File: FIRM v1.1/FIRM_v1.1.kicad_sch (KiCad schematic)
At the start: 79 parts, among them J2 Conn_01x02_Pin, Q1 IRLML6402, U10 STM32F446ZCHx, U3 ADXL371, U5 INA219AxDCN, U6 MIC5219-3.3YM5, U9 A-USBC-20F0-EA-GSR05, Y2 12 MHz

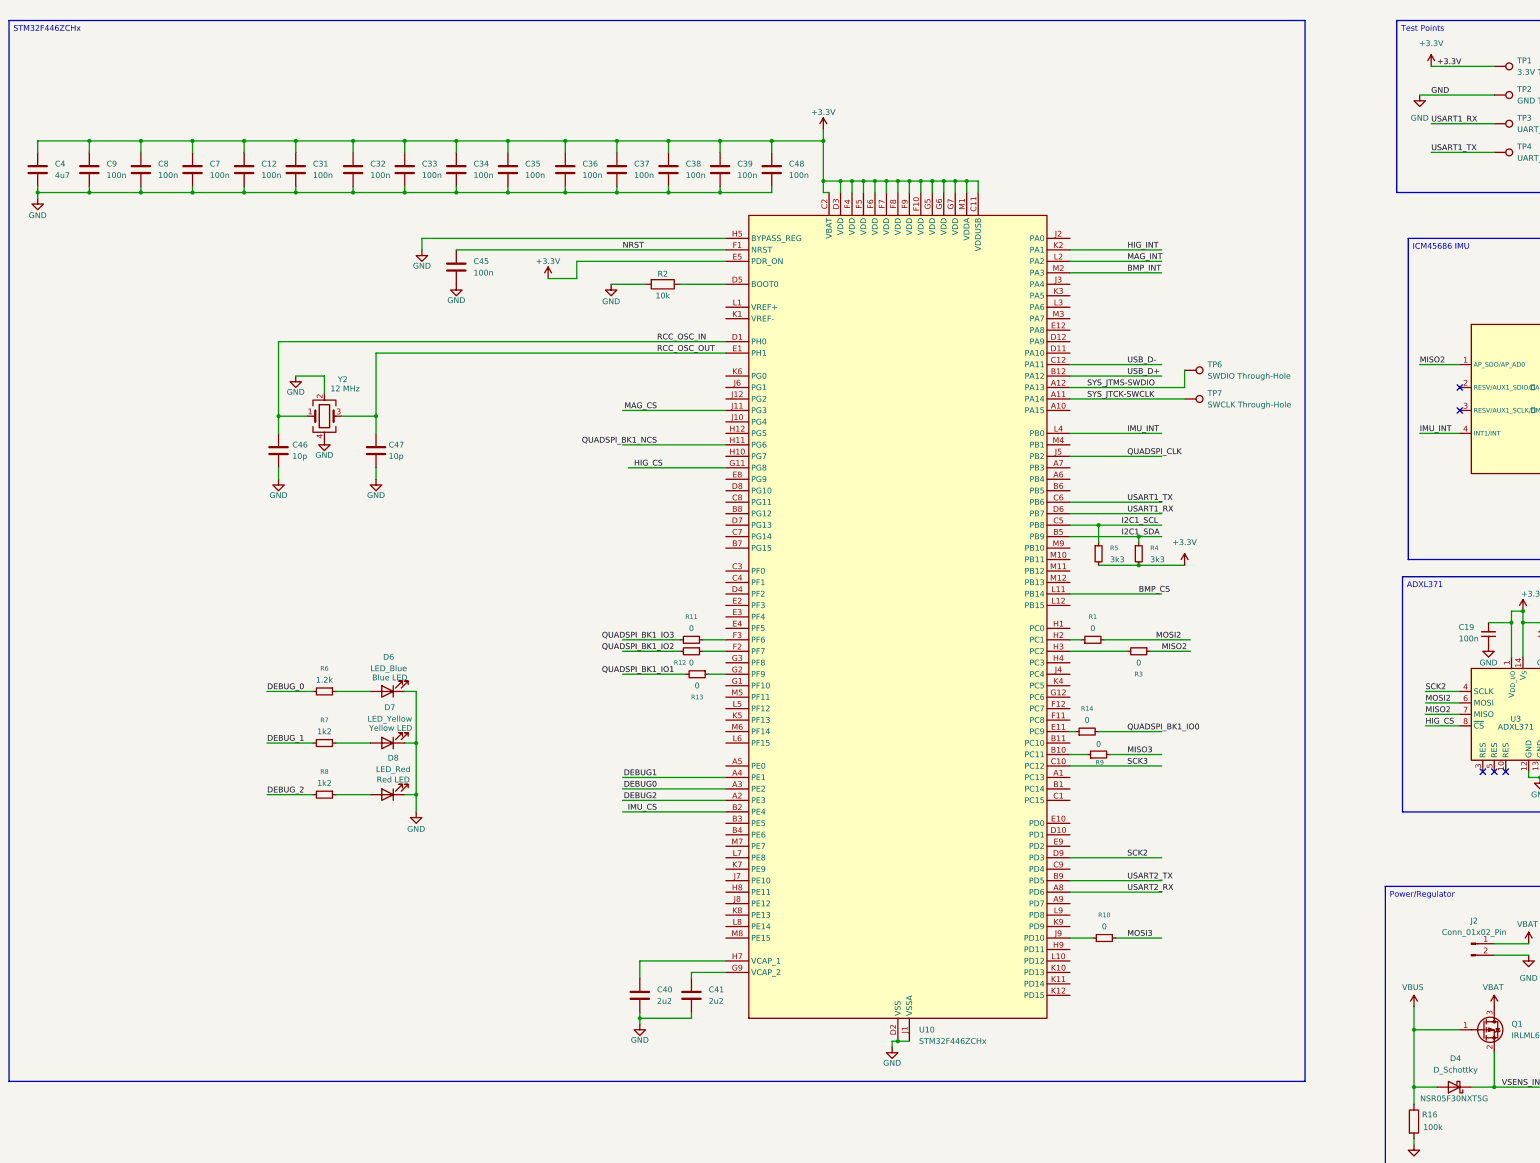
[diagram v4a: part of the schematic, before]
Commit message: Updated Pinout for STM and migrated schematics from shoe to 2.0
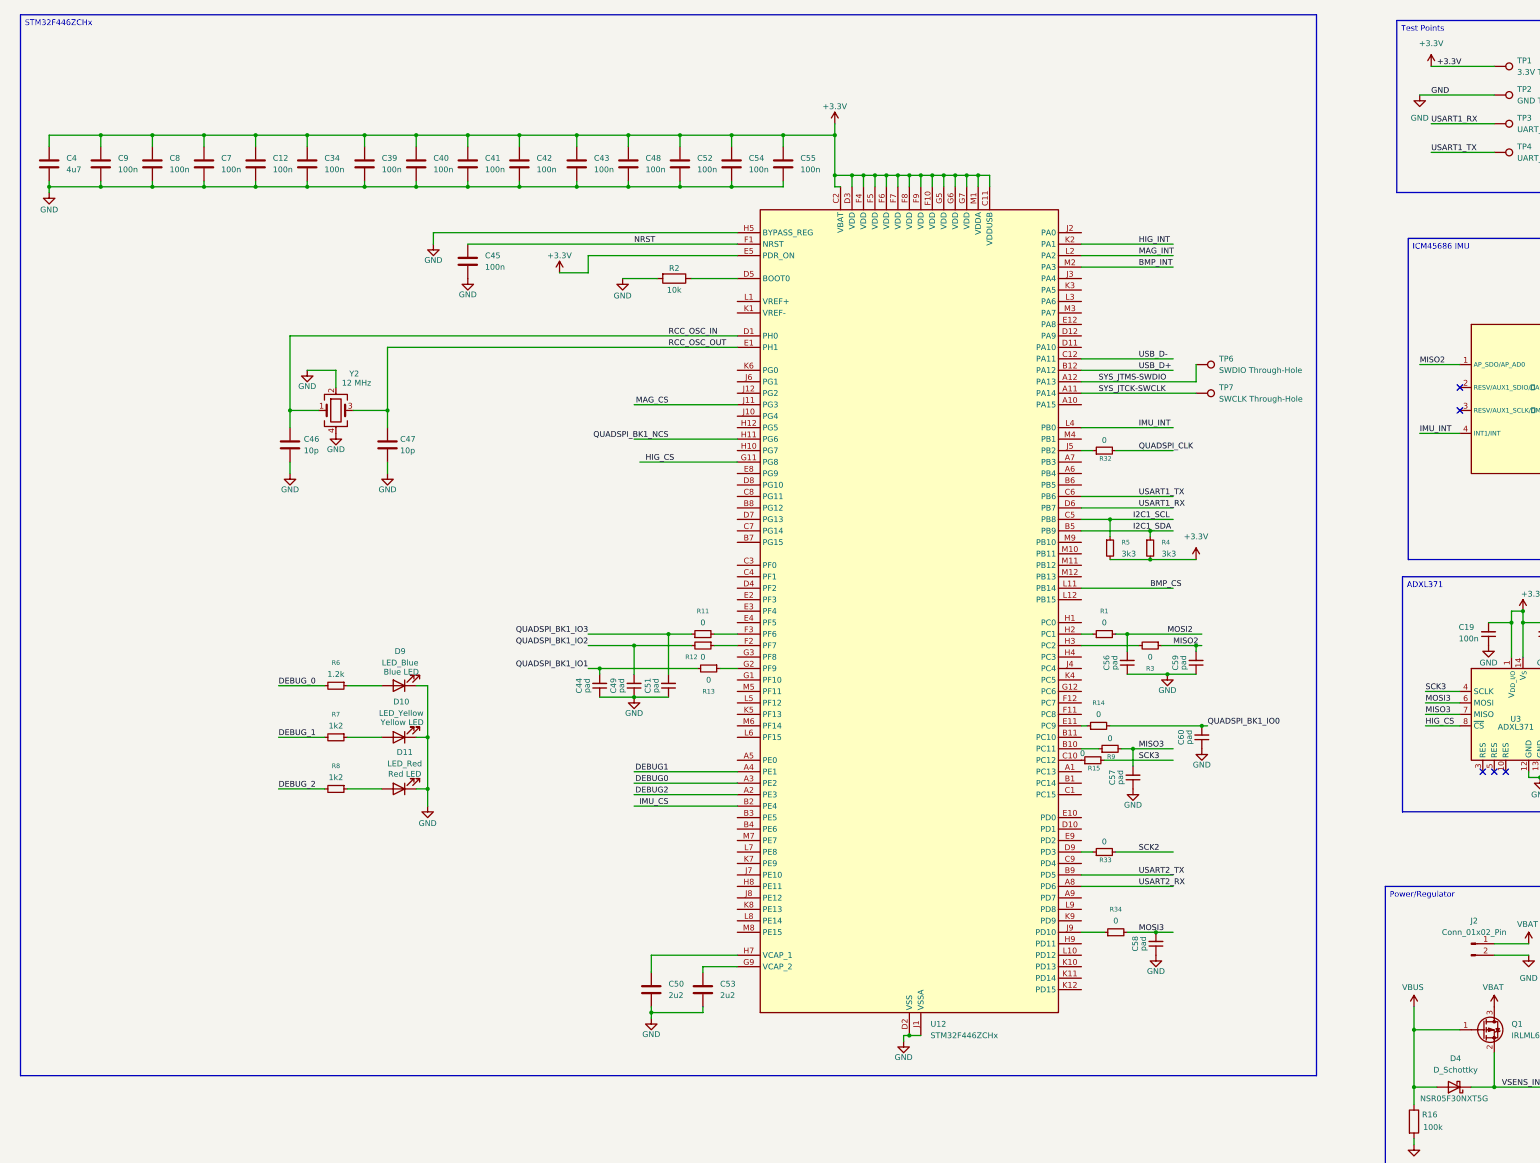
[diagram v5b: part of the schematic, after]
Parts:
- removed C31, C32, C33, C35, C36, C37, C38: 100n, Capacitor_SMD:C_0402_1005Metric, symbol Device:C
- removed D6: LED_Blue, LED_SMD:LED_0402_1005Metric, symbol Device:LED
- removed D7: LED_Yellow, LED_SMD:LED_0402_1005Metric, symbol Device:LED
- removed D8: LED_Red, LED_SMD:LED_0402_1005Metric, symbol Device:LED
- removed R10: 0, Package_DIP:DIP-8_W7.62mm, symbol Device:R_Small
- removed U10: STM32F446ZCHx, Package_BGA:UFBGA-144_7x7mm_Layout12x12_P0.5mm, symbol MCU_ST_STM32F4:STM32F446ZCHx
- added C42, C43, C52, C54, C55: 100n, Capacitor_SMD:C_0402_1005Metric, symbol Device:C
- added C44, C49, C51, C56, C57, C58, C59, C60: pad, Capacitor_SMD:C_0402_1005Metric, symbol Device:C_Small
- added C50, C53: 2u2, Capacitor_SMD:C_0402_1005Metric, symbol Device:C
- added D10: LED_Yellow, LED_SMD:LED_0402_1005Metric, symbol Device:LED
- added D11: LED_Red, LED_SMD:LED_0402_1005Metric, symbol Device:LED
- added D9: LED_Blue, LED_SMD:LED_0402_1005Metric, symbol Device:LED
- added R15, R32, R33, R34: 0, Package_DIP:DIP-8_W7.62mm, symbol Device:R_Small
- added U12: STM32F446ZCHx, Package_BGA:UFBGA-144_7x7mm_Layout12x12_P0.5mm, symbol MCU_ST_STM32F4:STM32F446ZCHx
- C40, C41: value 2u2 -> 100n; Digikey PN 490-10012-1-ND -> 1276-1043-1-ND; MPN C1607 -> C1590
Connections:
- net +3.3V: now also C40.1, C41.1, C42.1, C43.1, C52.1, C54.1, C55.1, U12.C11 (VDDUSB), U12.C2 (VBAT), U12.D3 (VDD), U12.E5 (PDR_ON), U12.F10 (VDD), U12.F4 (VDD), U12.F5 (VDD), U12.F6 (VDD), U12.F7 (VDD), U12.F8 (VDD), U12.F9 (VDD), U12.G5 (VDD), U12.G6 (VDD), U12.G7 (VDD), U12.M1 (VDDA)
- net BMP_CS: now also U12.L11 (PB14)
- net BMP_INT: now also U12.M2 (PA3)
- net DEBUG0: now also U12.A3 (PE2)
- net DEBUG1: now also U12.A4 (PE1)
- net DEBUG2: now also U12.A2 (PE3)
- net GND: now also C42.2, C43.2, C44.1, C49.1, C50.2, C51.1, C52.2, C53.2, C54.2, C55.2, C56.1, C57.1, C58.1, C59.1, C60.1, D10.1 (K), D11.1 (K), D9.1 (K), U12.D2 (VSS), U12.E6 (VSS), U12.E7 (VSS), U12.G10 (VSS), U12.G4 (VSS), U12.G8 (VSS), U12.H5 (BYPASS_REG), U12.H6 (VSS), U12.J1 (VSSA)
- net HIG_CS: now also U12.G11 (PG8)
- net HIG_INT: now also U12.K2 (PA1)
- net I2C1_SCL: now also U12.C5 (PB8)
- net I2C1_SDA: now also U12.B5 (PB9)
- net IMU_CS: now also U12.B2 (PE4)
- net IMU_INT: now also U12.L4 (PB0)
- net MAG_CS: now also U12.J11 (PG3)
- net MAG_INT: now also U12.L2 (PA2)
- net MISO2: now also C59.2; no longer U3.7 (MISO)
- net MISO3: now also U3.7 (MISO), C57.2
- net MOSI2: now also C56.2; no longer U3.6 (MOSI)
- net MOSI3: now also U3.6 (MOSI), C58.2, R34.2
- net NRST: now also U12.F1 (NRST)
- net QUADSPI_BK1_IO0: now also C60.2
- net QUADSPI_BK1_IO1: now also C44.2
- net QUADSPI_BK1_IO2: now also C49.2
- net QUADSPI_BK1_IO3: now also C51.2
- net QUADSPI_BK1_NCS: now also U12.H11 (PG6)
- net QUADSPI_CLK: now also R32.2
- net RCC_OSC_IN: now also U12.D1 (PH0)
- net RCC_OSC_OUT: now also U12.E1 (PH1)
- net SCK2: now also R33.2; no longer U3.4 (SCLK)
- net SCK3: now also U3.4 (SCLK), R15.2
- net SYS_JTCK-SWCLK: now also U12.A11 (PA14)
- net SYS_JTMS-SWDIO: now also U12.A12 (PA13)
- net USART1_RX: now also U12.D6 (PB7)
- net USART1_TX: now also U12.C6 (PB6)
- net USART2_RX: now also U12.A8 (PD6)
- net USART2_TX: now also U12.B9 (PD5)
- net USB_D+: now also U12.B12 (PA12)
- net USB_D-: now also U12.C12 (PA11)
- net at R3.2: now also U12.H3 (PC2)
- net at R6.1: now also D9.2 (A)
- net at R7.1: now also D10.2 (A)
- net at R8.1: now also D11.2 (A)
- net at R13.1: now also U12.G2 (PF9)
- net at R1.1: now also U12.H2 (PC1)
- net at R14.1: now also U12.E11 (PC9)
- net at R11.2: now also U12.F3 (PF6)
- net at R9.1: now also U12.B10 (PC11)
- net at R2.1: now also U12.D5 (BOOT0)
- net at R12.1: now also U12.F2 (PF7)
- new net: R15.1, U12.C10 (PC12)
- new net: R33.1, U12.D9 (PD3)
- new net: C53.1, U12.G9 (VCAP_2)
- new net: C50.1, U12.H7 (VCAP_1)
- new net: R32.1, U12.J5 (PB2)
- new net: R34.1, U12.J9 (PD10)
- new net: U3.10 (RES), U3.13 (GND), U3.16 (GND)
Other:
- company: Seth O, Will S, Harshil M, Jackson E -> Emmanuel RM, Will S, William D
- title: FIRM -> FIRM 1.1

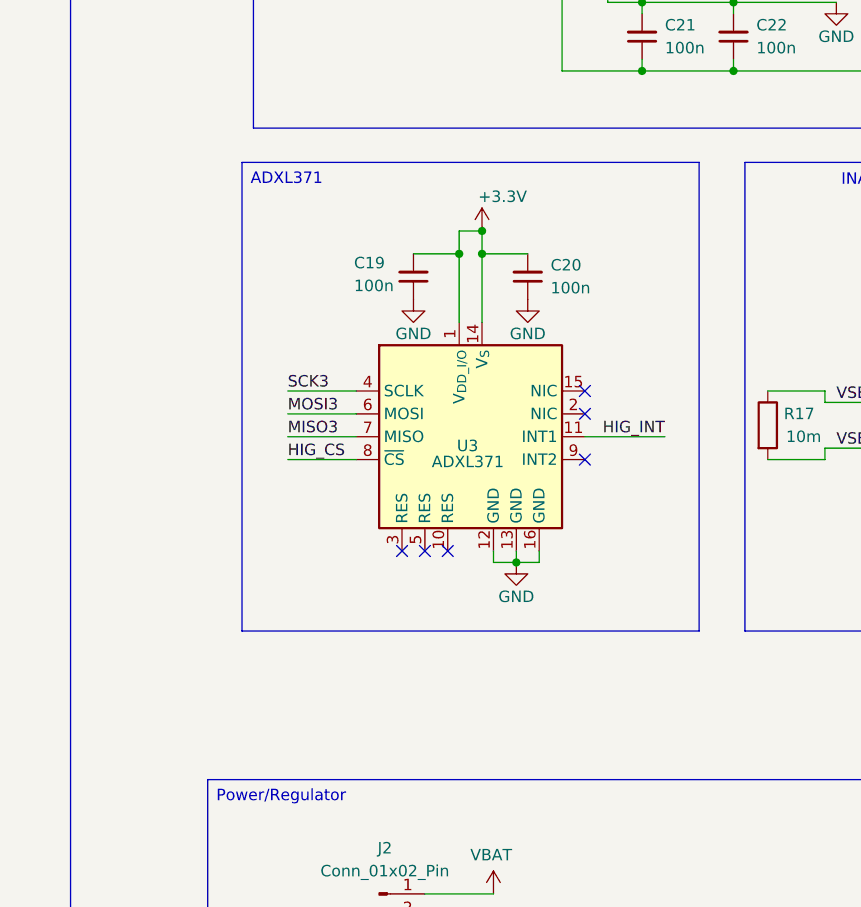
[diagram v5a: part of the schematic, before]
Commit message: Wired up ADXL375
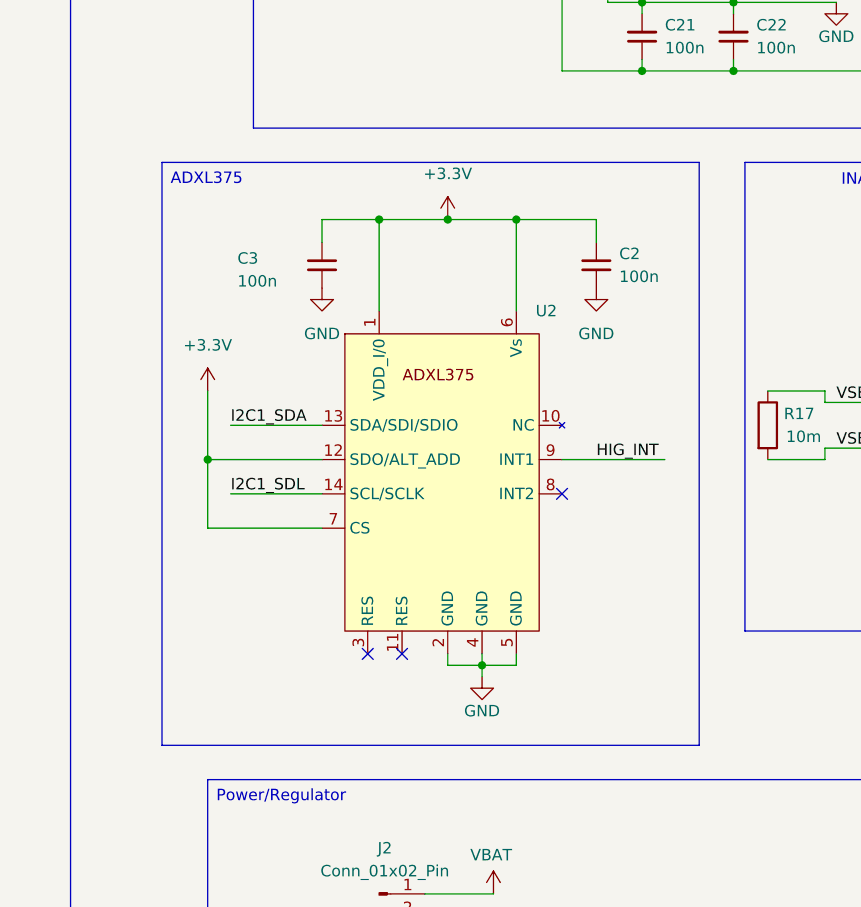
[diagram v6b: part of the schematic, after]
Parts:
- removed C19, C20: 100n, Capacitor_SMD:C_0402_1005Metric, symbol Device:C_Small
- removed U3: ADXL371, Sensor_Motion:Analog_LGA-16_3.25x3mm_P0.5mm_LayoutBorder3x5y, symbol Sensor_Motion:ADXL363
- added C2, C3: 100n, HPRC_Sensors:ADXL375BCCZ-RL7, symbol Device:C_Small
- added U2: (no value), HPRC_Sensors:ADXL375BCCZ-RL7, symbol HPRC_Sensors:ADXL375
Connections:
- net +3.3V: now also C2.1, C3.1, U2.1 (VDD_I/0), U2.12 (SDO/ALT_ADD), U2.6 (Vs), U2.7 (CS)
- net GND: now also C2.2, C3.2, U2.2 (GND), U2.4 (GND), U2.5 (GND)
- net HIG_INT: now also U2.9 (INT1)
- net I2C1_SDA: now also U2.13 (SDA/SDI/SDIO)
- new net I2C1_SDL: U2.14 (SCL/SCLK)
- no-connect marks 20 -> 17

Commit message: Wired up MIC216 and a third DEBUG LED
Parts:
- removed C26: 470p, Capacitor_SMD:C_0402_1005Metric, symbol Device:C_Small
- removed U6: MIC5219-3.3YM5, Package_TO_SOT_SMD:SOT-23-5, symbol Regulator_Linear:MIC5219-3.3YM5
- added D12: LED_Red, LED_SMD:LED_0402_1005Metric, symbol Device:LED
- added R10: 1k2, Resistor_SMD:R_0402_1005Metric, symbol Device:R_Small
- added R19: 100k, Resistor_SMD:R_0402_1005Metric, symbol Device:R_Small
- added U3: (no value), HPRC_regulators:MIC5216-3.3M5, symbol HPRC_Regulators:MIC5216-3.3YM5-TR
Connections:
- net +3.3V: now also U3.5 (OUT)
- net DEBUG0: now also U12.A4 (PE1); no longer U12.A3 (PE2)
- net DEBUG1: now also U12.A3 (PE2); no longer U12.A4 (PE1)
- net GND: now also D12.1 (K), U3.2 (GND)
- net VSENS_OUT: now also R19.2, U3.1 (IN), U3.3 (EN)
- net DEBUG3: now reaches U12.A1 (PC13)
- net DEBUG3: now also R10.2
- new net: D12.2 (A), R10.1
- new net MIC_FLAG: R19.1, U3.4 (FLG)
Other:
- moved on the sheet: C24

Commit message: Typo :p
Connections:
- net DEBUG3 renamed DEBUG_3
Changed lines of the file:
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@@
 		)
 	)
-	(label "DEBUG3"
+	(label "DEBUG_3"
 		(at 81.28 198.12 180)
 		(effects
@@
 		)
 	)
-	(label "DEBUG3"
+	(label "DEBUG_3"
 		(at 266.7 194.31 180)
 		(effects
